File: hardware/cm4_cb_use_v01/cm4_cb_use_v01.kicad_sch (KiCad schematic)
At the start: 0 parts

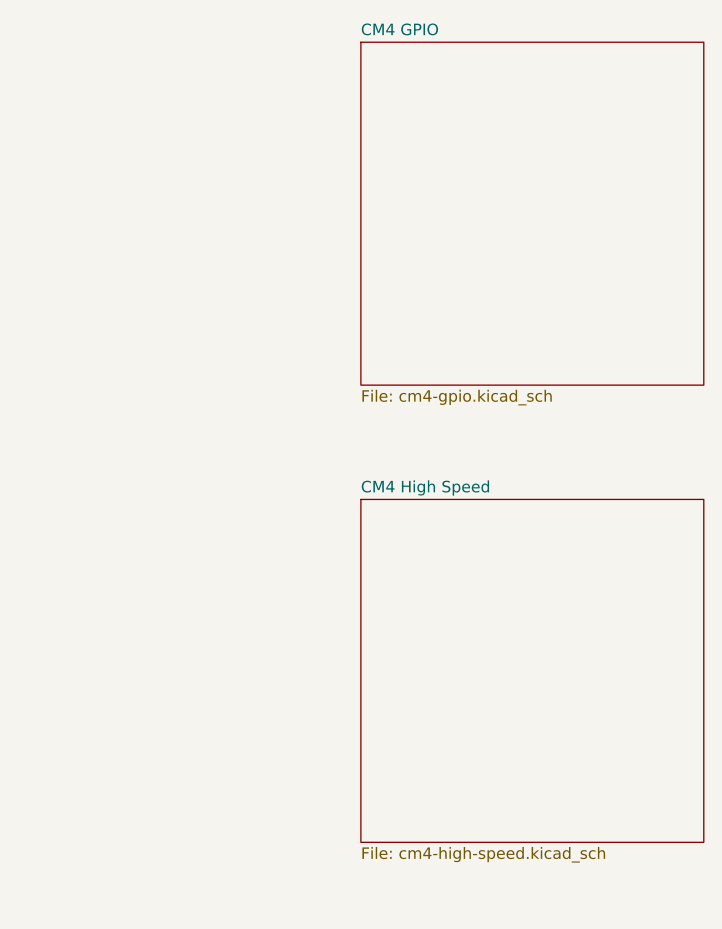
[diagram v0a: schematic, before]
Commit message: added usb-c and hdmi
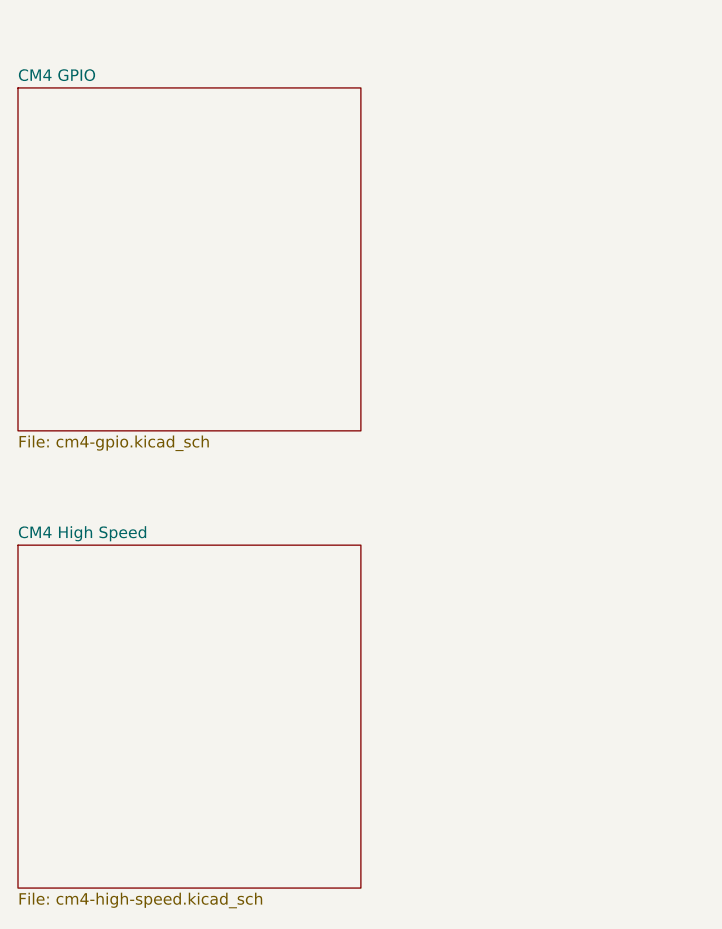
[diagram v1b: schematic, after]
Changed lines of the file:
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@@
     (comment 4 "Author: Martin Mæland")
   )
-  (sheet (at 101.6 50.8) (size 38.1 38.1)
+  (sheet (at 63.5 55.88) (size 38.1 38.1)
     (stroke (width 0) (type solid) (color 132 0 132 1))
     (fill (color 255 255 255 0.0000))
-    (property "Sheet name" "CM4 GPIO" (id 0) (at 101.6 50.1645 0)
+    (property "Sheet name" "CM4 GPIO" (id 0) (at 63.5 55.2445 0)
       (effects (font (size 1.27 1.27)) (justify left bottom))
     )
-    (property "Sheet file" "cm4-gpio.kicad_sch" (id 1) (at 101.6 89.4085 0)
+    (property "Sheet file" "cm4-gpio.kicad_sch" (id 1) (at 63.5 94.4885 0)
       (effects (font (size 1.27 1.27)) (justify left top))
     )
   )
-  (sheet (at 101.6 101.6) (size 38.1 38.1)
+  (sheet (at 63.5 106.68) (size 38.1 38.1)
     (stroke (width 0) (type solid) (color 132 0 132 1))
     (fill (color 255 255 255 0.0000))
-    (property "Sheet name" "CM4 High Speed" (id 0) (at 101.6 100.9645 0)
+    (property "Sheet name" "CM4 High Speed" (id 0) (at 63.5 106.0445 0)
       (effects (font (size 1.27 1.27)) (justify left bottom))
     )
-    (property "Sheet file" "cm4-high-speed.kicad_sch" (id 1) (at 101.6 140.2085 0)
+    (property "Sheet file" "cm4-high-speed.kicad_sch" (id 1) (at 63.5 145.2885 0)
       (effects (font (size 1.27 1.27)) (justify left top))
     )
@@
       (reference "#PWR0103") (unit 1) (value "GND") (footprint "")
     )
-    (path "/fc4c71a5-1008-4ac4-98db-57c838c57d91/48a5923e-2cf9-4b7b-b160-cc99f74e0c07"
-      (reference "#PWR0104") (unit 1) (value "GND") (footprint "")
-    )
     (path "/fc4c71a5-1008-4ac4-98db-57c838c57d91/e25b8971-e0e8-46aa-8cce-b4039a1b245b"
       (reference "#PWR0105") (unit 1) (value "GND") (footprint "")
-    )
-    (path "/fc4c71a5-1008-4ac4-98db-57c838c57d91/6dd8eb14-87a0-47a4-a592-50d45f3efdd0"
-      (reference "#PWR0106") (unit 1) (value "GND") (footprint "")
-    )
-    (path "/fc4c71a5-1008-4ac4-98db-57c838c57d91/8621ede0-801d-408a-ace1-9c9b631053c3"
-      (reference "#PWR0107") (unit 1) (value "GND") (footprint "")
-    )
-    (path "/fc4c71a5-1008-4ac4-98db-57c838c57d91/a517cd89-6381-470a-b34a-d194901e06fb"
-      (reference "#PWR0108") (unit 1) (value "GND") (footprint "")
     )
     (path "/fc4c71a5-1008-4ac4-98db-57c838c57d91/b2bdacc5-5dd7-4aea-ae1d-b1028ef0bfb1"
       (reference "#PWR0110") (unit 1) (value "GND") (footprint "")
     )
-    (path "/fc4c71a5-1008-4ac4-98db-57c838c57d91/fbc197bf-e2f3-4638-9935-f28d7c075a1e"
-      (reference "CR1") (unit 1) (value "SMBJ5.0A-TR") (footprint "footprints:SMBJ5.0A-TR")
-    )
     (path "/fc4c71a5-1008-4ac4-98db-57c838c57d91/a7ffff95-46ae-494c-85c4-9efe00fc8a49"
-      (reference "D1") (unit 1) (value "LED Green") (footprint "LED_SMD:LED_0603_1608Metric")
+      (reference "D1") (unit 1) (value "LED Green") (footprint "LED_SMD:LED_0805_2012Metric")
     )
     (path "/fc4c71a5-1008-4ac4-98db-57c838c57d91/12d78f79-203c-4c00-81dd-cf0e4083b575"
-      (reference "D2") (unit 1) (value "LED Red") (footprint "LED_SMD:LED_0603_1608Metric")
+      (reference "D2") (unit 1) (value "LED Red") (footprint "LED_SMD:LED_0805_2012Metric")
     )
     (path "/fc4c71a5-1008-4ac4-98db-57c838c57d91/7daa98ed-9d74-497f-a5b7-7cb922441ba1"
       (reference "J1") (unit 1) (value "DNP") (footprint "Connector_PinHeader_2.54mm:PinHeader_1x10_P2.54mm_Vertical")
-    )
-    (path "/fc4c71a5-1008-4ac4-98db-57c838c57d91/1591dea8-b19a-4d2f-8baa-e66d31282c58"
-      (reference "J2") (unit 1) (value "USB4105-GF-A") (footprint "USB4105-GF-A:GCT_USB4105-GF-A")
     )
     (path "/fc4c71a5-1008-4ac4-98db-57c838c57d91/e653ed96-2ceb-42bc-905c-db47449cc067"
@@
       (reference "Module1") (unit 1) (value "ComputeModule4-CM4") (footprint "CM4IO:Raspberry-Pi-4-Compute-Module")
     )
-    (path "/fc4c71a5-1008-4ac4-98db-57c838c57d91/19ae9b22-a1d3-4ec4-a43e-6fb99c903f21"
-      (reference "R1") (unit 1) (value "5.1k") (footprint "Resistor_SMD:R_0603_1608Metric_Pad0.98x0.95mm_HandSolder")
+    (path "/fc4c71a5-1008-4ac4-98db-57c838c57d91/0cf35274-d35b-4026-b08c-e45677951fcd"
+      (reference "R1") (unit 1) (value "1k") (footprint "Resistor_SMD:R_0805_2012Metric")
     )
     (path "/fc4c71a5-1008-4ac4-98db-57c838c57d91/bbc9e09d-42da-4f29-be94-2e044d09f397"
-      (reference "R2") (unit 1) (value "1k") (footprint "Resistor_SMD:R_0603_1608Metric_Pad0.98x0.95mm_HandSolder")
+      (reference "R2") (unit 1) (value "1k") (footprint "Resistor_SMD:R_0805_2012Metric")
     )
-    (path "/fc4c71a5-1008-4ac4-98db-57c838c57d91/e581bea2-a554-4309-85f8-e6e0ce07520c"
-      (reference "R4") (unit 1) (value "5.1k") (footprint "Resistor_SMD:R_0603_1608Metric_Pad0.98x0.95mm_HandSolder")
+    (path "/fc4c71a5-1008-4ac4-98db-57c838c57d91/a447d0d8-b88b-4096-b711-65a26c3df482"
+      (reference "U1") (unit 1) (value "SN74LVC1G07DCKR") (footprint "")
     )
-    (path "/fc4c71a5-1008-4ac4-98db-57c838c57d91/d38ddb23-f9c2-4a28-9fd8-d1fffee189f7"
-      (reference "R6") (unit 1) (value "1k") (footprint "Resistor_SMD:R_0603_1608Metric_Pad0.98x0.95mm_HandSolder")
+    (path "/caa71f4c-454d-4ac9-b287-456eafb34991/b2399ede-2d4f-433e-b8d4-681558150323"
+      (reference "#PWR0104") (unit 1) (value "GND") (footprint "")
     )
-    (path "/fc4c71a5-1008-4ac4-98db-57c838c57d91/862be61d-8399-4948-a564-2f01d5cb5b7a"
-      (reference "U1") (unit 1) (value "74LVC1G07SE-7") (footprint "Package_TO_SOT_SMD:SOT-353_SC-70-5")
+    (path "/caa71f4c-454d-4ac9-b287-456eafb34991/53033399-3431-4fde-b203-5ec4bce1f2b8"
+      (reference "#PWR0106") (unit 1) (value "GND") (footprint "")
+    )
+    (path "/caa71f4c-454d-4ac9-b287-456eafb34991/98b59a39-5dc3-4557-9fcf-3ae62de5a6dc"
+      (reference "#PWR0107") (unit 1) (value "GND") (footprint "")
     )
     (path "/caa71f4c-454d-4ac9-b287-456eafb34991/0d0caf91-4ece-48ed-a178-43a8b49f3526"
@@
       (reference "#PWR0112") (unit 1) (value "GND") (footprint "")
     )
-    (path "/caa71f4c-454d-4ac9-b287-456eafb34991/7aaeccae-7554-4237-a159-f19729377488"
-      (reference "#PWR0113") (unit 1) (value "GND") (footprint "")
-    )
-    (path "/caa71f4c-454d-4ac9-b287-456eafb34991/b2399ede-2d4f-433e-b8d4-681558150323"
-      (reference "#PWR?") (unit 1) (value "GND") (footprint "")
+    (path "/caa71f4c-454d-4ac9-b287-456eafb34991/0936af94-7709-4bc9-a27a-24e3243eece9"
+      (reference "J2") (unit 1) (value "HDMI_A") (footprint "")
     )
     (path "/caa71f4c-454d-4ac9-b287-456eafb34991/94c7d5d7-d648-439f-a208-c5670f7fe4ab"
-      (reference "J?") (unit 1) (value "1054500101") (footprint "Molex-1054500101-*")
+      (reference "J3") (unit 1) (value "1054500101") (footprint "")
     )
     (path "/caa71f4c-454d-4ac9-b287-456eafb34991/fafda8be-1326-444e-bcc1-8cb4aded3240"
@@
     )
     (path "/caa71f4c-454d-4ac9-b287-456eafb34991/396b9497-eaad-42f6-adc1-1d724e13ef1c"
-      (reference "R?") (unit 1) (value "2.2K 1%") (footprint "Resistor_SMD:R_0603_1608Metric_Pad0.98x0.95mm_HandSolder")
+      (reference "R3") (unit 1) (value "2.2K 1%") (footprint "Resistor_SMD:R_0603_1608Metric_Pad0.98x0.95mm_HandSolder")
     )
     (path "/caa71f4c-454d-4ac9-b287-456eafb34991/ceb61f80-9754-4184-938a-c0f30efebd07"
-      (reference "R?") (unit 1) (value "2.2K 1%") (footprint "Resistor_SMD:R_0603_1608Metric_Pad0.98x0.95mm_HandSolder")
+      (reference "R4") (unit 1) (value "2.2K 1%") (footprint "Resistor_SMD:R_0603_1608Metric_Pad0.98x0.95mm_HandSolder")
     )
     (path "/caa71f4c-454d-4ac9-b287-456eafb34991/25c200c8-8d48-421b-ac68-c53b8df4e956"
